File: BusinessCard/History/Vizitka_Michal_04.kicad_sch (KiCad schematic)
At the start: 29 parts, among them J1 USB_B_Micro, J2 USB_C_Receptacle, J3 Conn_01x01

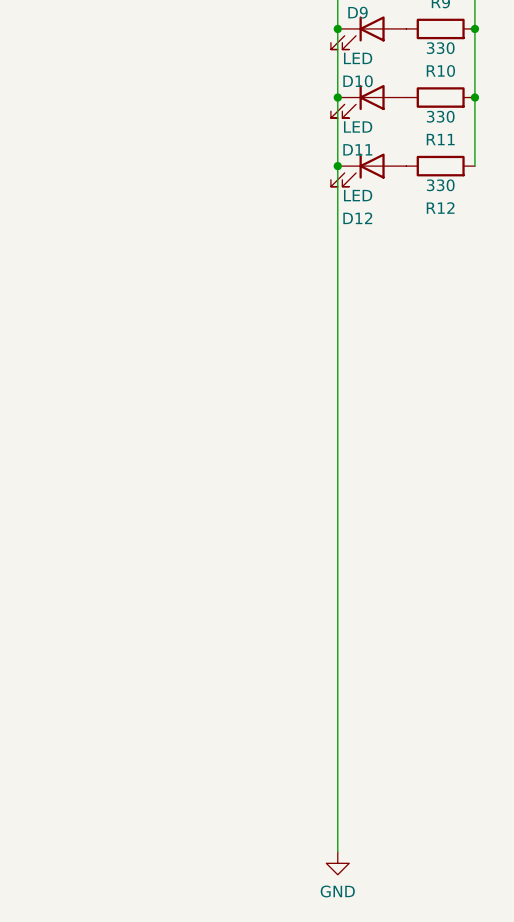
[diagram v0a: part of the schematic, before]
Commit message: Added aditional businesscards - Zuza, MichalModra...Actual Tapeout 2023-08-24, but repaired connection!
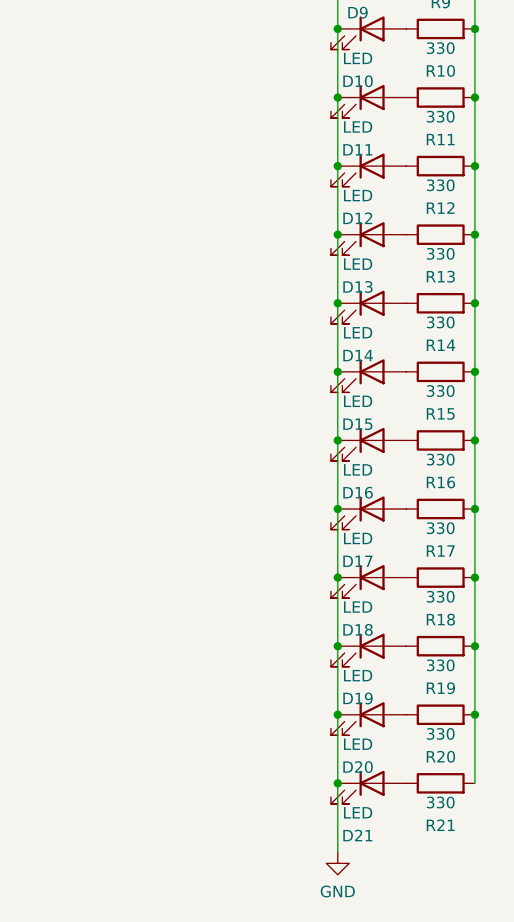
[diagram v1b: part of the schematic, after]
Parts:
- added D13, D14, D15, D16, D17, D18, D19, D20, D21: LED, meteopress:D_0402_woSilk, symbol Device:LED
- added R13, R14, R15, R16, R17, R18, R19, R20, R21: 330, meteopress:R_0201_woSilk, symbol Device:R
- D1, D10, D11, D12, D2, D3, D4, D5, D6, D7, D8, D9: footprint meteopress:D_0802_side_woSilk -> meteopress:D_0402_woSilk
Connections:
- net +5V: now also R13.2, R14.2, R15.2, R16.2, R17.2, R18.2, R19.2, R20.2, R21.2
- net GND: now also D13.1 (K), D14.1 (K), D15.1 (K), D16.1 (K), D17.1 (K), D18.1 (K), D19.1 (K), D20.1 (K), D21.1 (K)
- new net: D18.2 (A), R18.1
- new net: D17.2 (A), R17.1
- new net: D19.2 (A), R19.1
- new net: D16.2 (A), R16.1
- new net: D20.2 (A), R20.1
- new net: D14.2 (A), R14.1
- new net: D21.2 (A), R21.1
- new net: D13.2 (A), R13.1
- new net: D15.2 (A), R15.1
